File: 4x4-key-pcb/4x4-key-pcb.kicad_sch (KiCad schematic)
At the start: 57 parts, among them J2 Conn_01x05_Pin, SW1 SW_Push, U1 TPS62162DSG, U2 STM32G0B1KBTx, U3 SN65HVD230

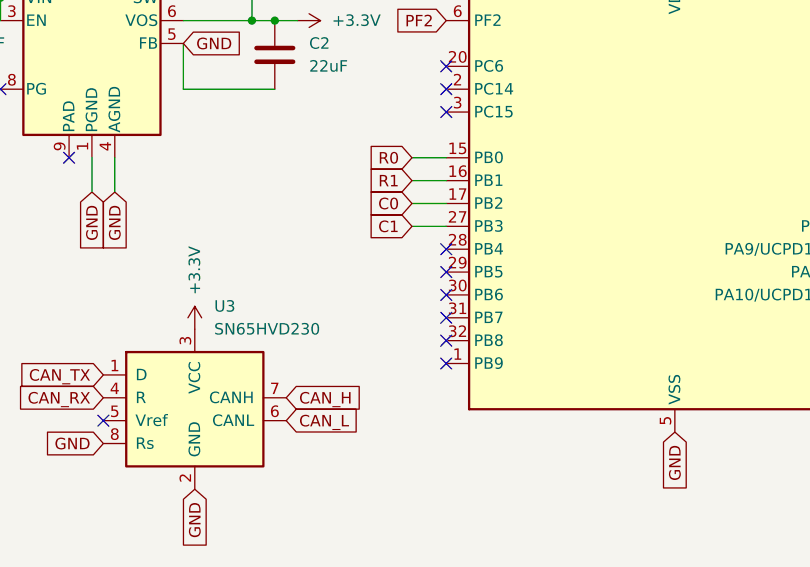
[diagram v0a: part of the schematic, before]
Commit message: routed 4x4 pad
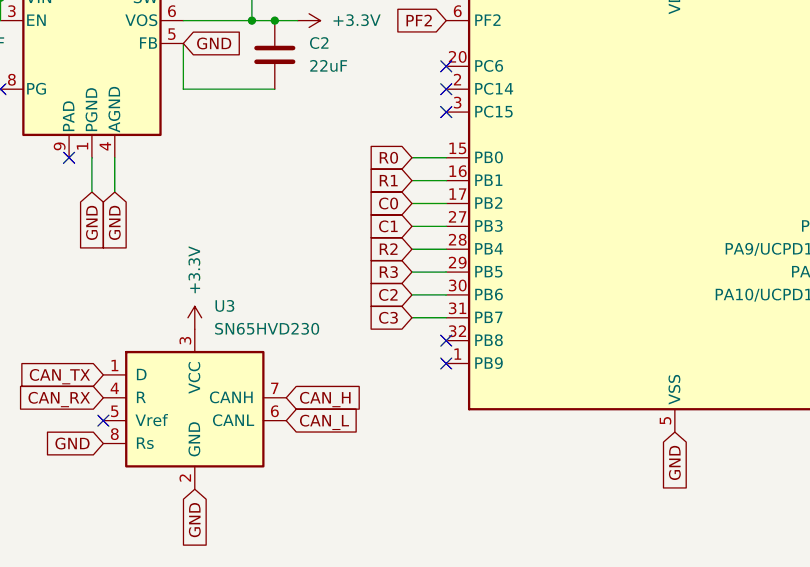
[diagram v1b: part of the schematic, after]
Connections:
- net C2: now also U2.30 (PB6)
- net C3: now also U2.31 (PB7)
- net R2: now also U2.28 (PB4)
- net R3: now also U2.29 (PB5)
- no-connect marks 19 -> 15
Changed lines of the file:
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@@
-	)
-	(no_connect
-		(at 80.01 58.42)
 	)
 	(no_connect
@@
 	)
 	(no_connect
-		(at 80.01 55.88)
-	)
-	(no_connect
 		(at 130.81 58.42)
 	)
@@
 	)
 	(no_connect
-		(at 80.01 60.96)
-	)
-	(no_connect
 		(at 80.01 35.56)
-	)
-	(no_connect
-		(at 80.01 53.34)
 	)
 	(no_connect
@@
 	(wire
 		(pts
+			(xy 76.2 58.42) (xy 80.01 58.42)
+		)
+		(stroke
+			(width 0)
+			(type default)
+		)
+	)
+	(wire
+		(pts
 			(xy 43.18 46.99) (xy 43.18 43.18)
 		)
@@
 	(wire
 		(pts
+			(xy 76.2 60.96) (xy 80.01 60.96)
+		)
+		(stroke
+			(width 0)
+			(type default)
+		)
+	)
+	(wire
+		(pts
 			(xy 91.44 114.3) (xy 99.06 114.3)
 		)
@@
 	(wire
 		(pts
+			(xy 76.2 53.34) (xy 80.01 53.34)
+		)
+		(stroke
+			(width 0)
+			(type default)
+		)
+	)
+	(wire
+		(pts
 			(xy 106.68 147.32) (xy 110.49 147.32)
 		)
@@
 	(wire
 		(pts
+			(xy 76.2 55.88) (xy 80.01 55.88)
+		)
+		(stroke
+			(width 0)
+			(type default)
+		)
+	)
+	(wire
+		(pts
 			(xy 78.74 104.14) (xy 78.74 120.65)
 		)
@@
 		)
 	)
+	(global_label "C3"
+		(shape input)
+		(at 76.2 60.96 180)
+		(fields_autoplaced yes)
+		(effects
+			(font
+				(size 1.27 1.27)
+			)
+			(justify right)
+		)
+		(property "Intersheetrefs" "${INTERSHEET_REFS}"
+			(at 70.7353 60.96 0)
+			(effects
+				(font
+					(size 1.27 1.27)
+				)
+				(justify right)
+				(hide yes)
+			)
+		)
+	)
 	(global_label "GND"
 		(shape input)
@@
 		)
 	)
+	(global_label "R3"
+		(shape input)
+		(at 76.2 55.88 180)
+		(fields_autoplaced yes)
+		(effects
+			(font
+				(size 1.27 1.27)
+			)
+			(justify right)
+		)
+		(property "Intersheetrefs" "${INTERSHEET_REFS}"
+			(at 70.7353 55.88 0)
+			(effects
+				(font
+					(size 1.27 1.27)
+				)
+				(justify right)
+				(hide yes)
+			)
+		)
+	)
 	(global_label "+5V"
 		(shape input)
@@
 		)
 	)
+	(global_label "R2"
+		(shape input)
+		(at 76.2 53.34 180)
+		(fields_autoplaced yes)
+		(effects
+			(font
+				(size 1.27 1.27)
+			)
+			(justify right)
+		)
+		(property "Intersheetrefs" "${INTERSHEET_REFS}"
+			(at 70.7353 53.34 0)
+			(effects
+				(font
+					(size 1.27 1.27)
+				)
+				(justify right)
+				(hide yes)
+			)
+		)
+	)
 	(global_label "CS"
 		(shape input)
@@
 			(effects
 				(font
+					(size 1.27 1.27)
+				)
+				(justify right)
+				(hide yes)
+			)
+		)
+	)
+	(global_label "C2"
+		(shape input)
+		(at 76.2 58.42 180)
+		(fields_autoplaced yes)
+		(effects
+			(font
+				(size 1.27 1.27)
+			)
+			(justify right)
+		)
+		(property "Intersheetrefs" "${INTERSHEET_REFS}"
+			(at 70.7353 58.42 0)
+			(effects
+				(font
